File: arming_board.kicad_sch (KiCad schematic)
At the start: 31 parts, among them IC1 CD4043BDR, J3 Conn_01x04, Q2 SQJ409EP

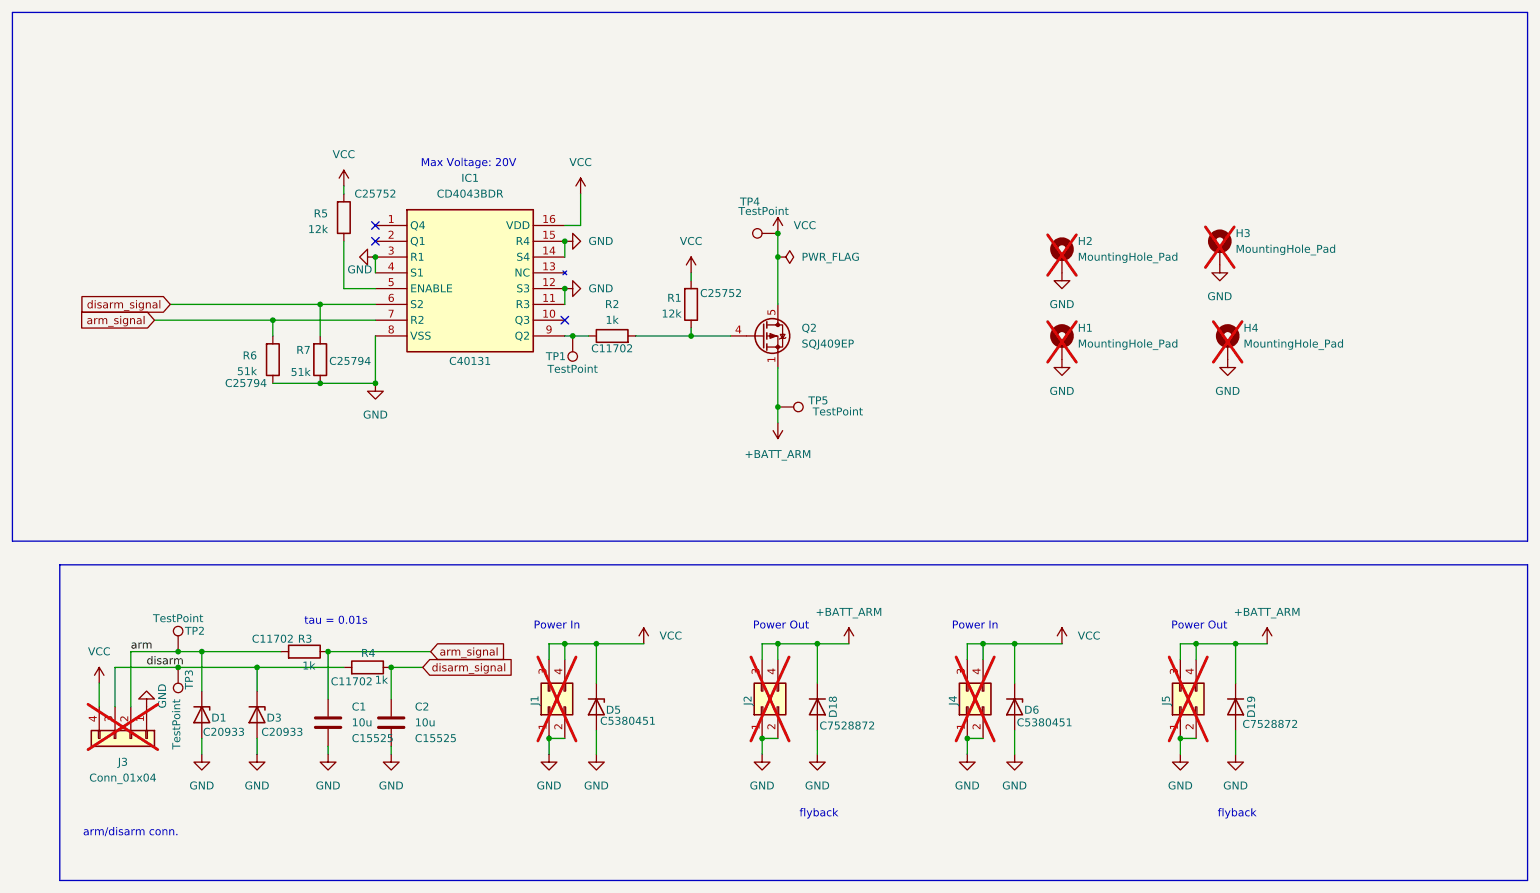
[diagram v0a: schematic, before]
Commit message: cleanup repo and export 3D model
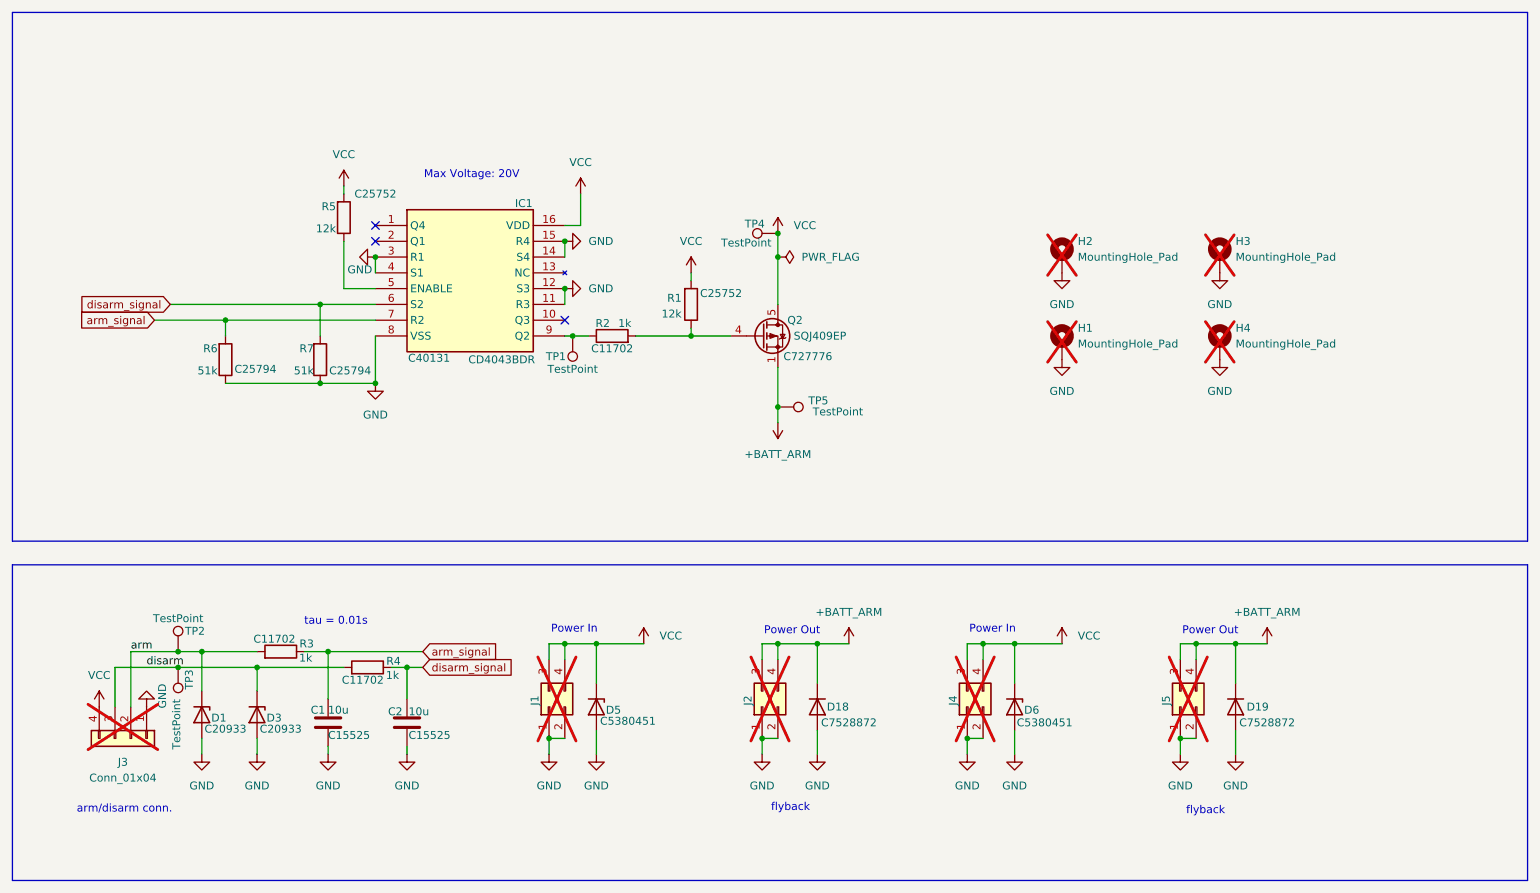
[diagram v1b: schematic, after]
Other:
- title: (none) -> Arming Board
- moved on the sheet: C2, H3, H4, R3, R6

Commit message: fix mosfet
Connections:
- net +BATT_ARM: now also Q2.5 (D); no longer Q2.1 (S), Q2.2 (S), Q2.3 (S)
- net VCC: now also Q2.1 (S), Q2.2 (S), Q2.3 (S); no longer Q2.5 (D)
